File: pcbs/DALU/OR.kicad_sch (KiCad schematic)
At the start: 3 parts, among them U701 74HC32, U702 74HC32, U703 74HC245

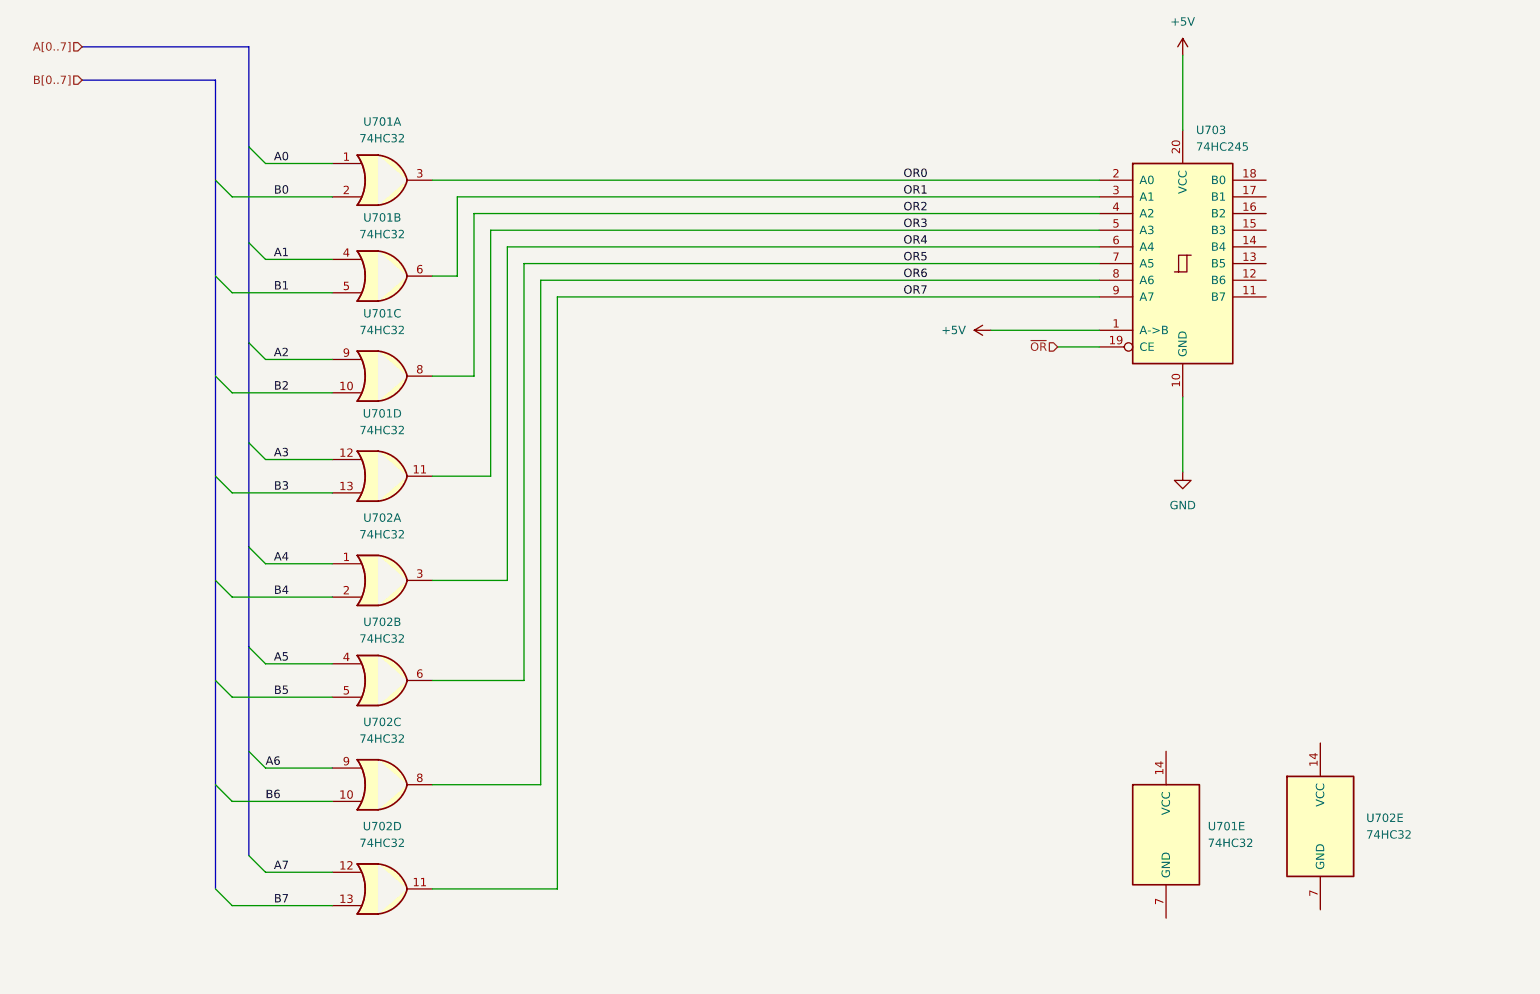
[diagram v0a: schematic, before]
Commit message: Routing.... have realised that I need to think more about vias
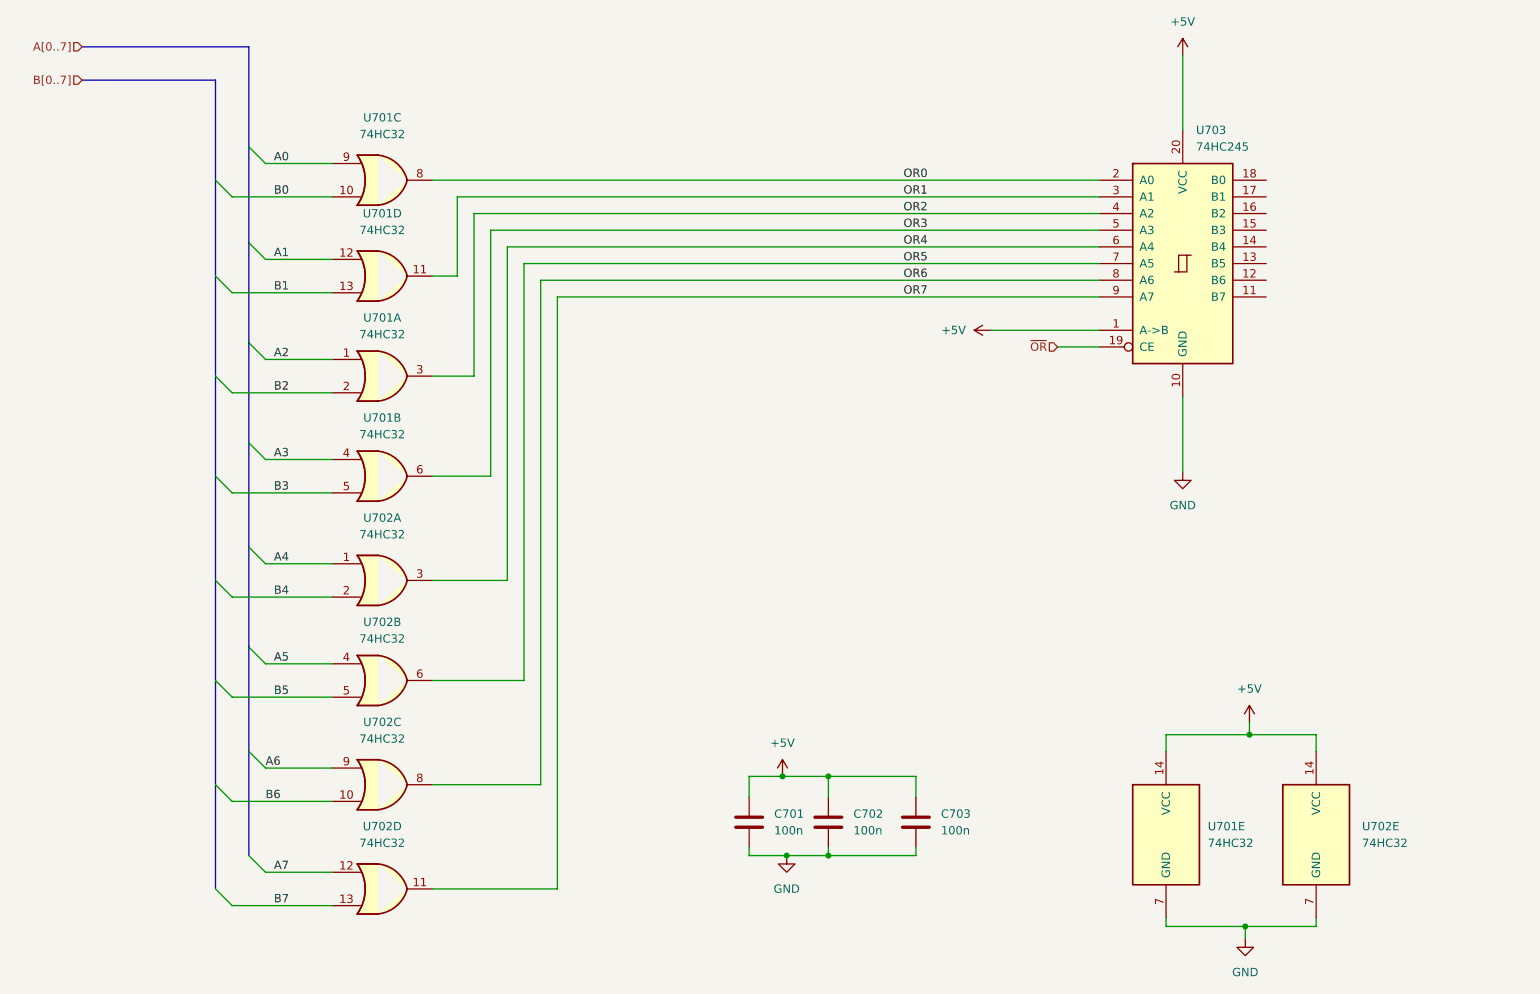
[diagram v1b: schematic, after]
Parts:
- added C701, C702, C703: 100n, Capacitor_SMD:C_0603_1608Metric, symbol Device:C
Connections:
- net +5V: now also U701.14 (VCC), U702.14 (VCC), C701.1, C702.1, C703.1
- net A0: now also U701.9; no longer U701.1
- net A1: now also U701.12; no longer U701.4
- net A2: now also U701.1; no longer U701.9
- net A3: now also U701.4; no longer U701.12
- net B0: now also U701.10; no longer U701.2
- net B1: now also U701.13; no longer U701.5
- net B2: now also U701.2; no longer U701.10
- net B3: now also U701.5; no longer U701.13
- net GND: now also U701.7 (GND), U702.7 (GND), C701.2, C702.2, C703.2
- net OR0: now also U701.8; no longer U701.3
- net OR1: now also U701.11; no longer U701.6
- net OR2: now also U701.3; no longer U701.8
- net OR3: now also U701.6; no longer U701.11
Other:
- moved on the sheet: U701A, U701B, U701C, U701D, U702E

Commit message: More rerouting
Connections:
- net RESULT7: now reaches U703.11 (B7)
- net RESULT6: now reaches U703.12 (B6)
- net RESULT5: now reaches U703.13 (B5)
- net RESULT4: now reaches U703.14 (B4)
- net RESULT3: now reaches U703.15 (B3)
- net RESULT2: now reaches U703.16 (B2)
- net RESULT1: now reaches U703.17 (B1)
- net RESULT0: now reaches U703.18 (B0)
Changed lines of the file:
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@@
   (junction (at 215.9 130.175) (diameter 0) (color 0 0 0 0)
   )
+  (bus_entry (at 234.315 60.96) (size -2.54 2.54)
+    (stroke (width 0) (type default) (color 0 0 0 0))
+  )
+  (bus_entry (at 234.315 53.34) (size -2.54 2.54)
+    (stroke (width 0) (type default) (color 0 0 0 0))
+  )
   (bus_entry (at 63.5 70.485) (size 2.54 2.54)
     (stroke (width 0) (type default) (color 0 0 0 0))
   )
+  (bus_entry (at 234.315 43.18) (size -2.54 2.54)
+    (stroke (width 0) (type default) (color 0 0 0 0))
+  )
   (bus_entry (at 58.42 106.68) (size 2.54 2.54)
     (stroke (width 0) (type default) (color 0 0 0 0))
   )
+  (bus_entry (at 234.315 58.42) (size -2.54 2.54)
+    (stroke (width 0) (type default) (color 0 0 0 0))
+  )
   (bus_entry (at 63.5 55.245) (size 2.54 2.54)
     (stroke (width 0) (type default) (color 0 0 0 0))
@@
     (stroke (width 0) (type default) (color 0 0 0 0))
   )
+  (bus_entry (at 234.315 45.72) (size -2.54 2.54)
+    (stroke (width 0) (type default) (color 0 0 0 0))
+  )
   (bus_entry (at 63.5 132.715) (size 2.54 2.54)
     (stroke (width 0) (type default) (color 0 0 0 0))
@@
     (stroke (width 0) (type default) (color 0 0 0 0))
   )
+  (bus_entry (at 234.315 48.26) (size -2.54 2.54)
+    (stroke (width 0) (type default) (color 0 0 0 0))
+  )
   (bus_entry (at 58.42 121.92) (size 2.54 2.54)
     (stroke (width 0) (type default) (color 0 0 0 0))
   )
+  (bus_entry (at 234.315 55.88) (size -2.54 2.54)
+    (stroke (width 0) (type default) (color 0 0 0 0))
+  )
   (bus_entry (at 58.42 45.72) (size 2.54 2.54)
     (stroke (width 0) (type default) (color 0 0 0 0))
@@
     (stroke (width 0) (type default) (color 0 0 0 0))
   )
+  (bus_entry (at 234.315 50.8) (size -2.54 2.54)
+    (stroke (width 0) (type default) (color 0 0 0 0))
+  )
   (wire (pts (xy 91.44 121.92) (xy 105.41 121.92))
     (stroke (width 0) (type default) (color 0 0 0 0))
   )
+  (bus (pts (xy 234.315 48.26) (xy 234.315 50.8))
+    (stroke (width 0) (type default) (color 0 0 0 0))
+  )
   (wire (pts (xy 91.44 60.325) (xy 95.25 60.325))
     (stroke (width 0) (type default) (color 0 0 0 0))
@@
     (stroke (width 0) (type default) (color 0 0 0 0))
   )
+  (wire (pts (xy 218.44 55.88) (xy 231.775 55.88))
+    (stroke (width 0) (type default) (color 0 0 0 0))
+  )
+  (wire (pts (xy 218.44 53.34) (xy 231.775 53.34))
+    (stroke (width 0) (type default) (color 0 0 0 0))
+  )
   (bus (pts (xy 58.42 137.795) (xy 58.42 153.67))
     (stroke (width 0) (type default) (color 0 0 0 0))
@@
     (stroke (width 0) (type default) (color 0 0 0 0))
   )
+  (wire (pts (xy 218.44 58.42) (xy 231.775 58.42))
+    (stroke (width 0) (type default) (color 0 0 0 0))
+  )
   (wire (pts (xy 165.1 136.525) (xy 165.1 139.7))
     (stroke (width 0) (type default) (color 0 0 0 0))
@@
     (stroke (width 0) (type default) (color 0 0 0 0))
   )
+  (bus (pts (xy 234.315 55.88) (xy 234.315 58.42))
+    (stroke (width 0) (type default) (color 0 0 0 0))
+  )
   (wire (pts (xy 107.95 137.795) (xy 91.44 137.795))
     (stroke (width 0) (type default) (color 0 0 0 0))
@@
     (stroke (width 0) (type default) (color 0 0 0 0))
   )
+  (bus (pts (xy 234.315 58.42) (xy 234.315 60.96))
+    (stroke (width 0) (type default) (color 0 0 0 0))
+  )
   (wire (pts (xy 60.96 140.335) (xy 76.2 140.335))
     (stroke (width 0) (type default) (color 0 0 0 0))
@@
     (stroke (width 0) (type default) (color 0 0 0 0))
   )
+  (wire (pts (xy 218.44 63.5) (xy 231.775 63.5))
+    (stroke (width 0) (type default) (color 0 0 0 0))
+  )
+  (bus (pts (xy 234.315 36.83) (xy 234.315 43.18))
+    (stroke (width 0) (type default) (color 0 0 0 0))
+  )
   (bus (pts (xy 63.5 101.6) (xy 63.5 116.84))
     (stroke (width 0) (type default) (color 0 0 0 0))
@@
     (stroke (width 0) (type default) (color 0 0 0 0))
   )
+  (bus (pts (xy 234.315 43.18) (xy 234.315 45.72))
+    (stroke (width 0) (type default) (color 0 0 0 0))
+  )
+  (wire (pts (xy 218.44 48.26) (xy 231.775 48.26))
+    (stroke (width 0) (type default) (color 0 0 0 0))
+  )
   (wire (pts (xy 145.415 148.59) (xy 151.765 148.59))
     (stroke (width 0) (type default) (color 0 0 0 0))
@@
     (stroke (width 0) (type default) (color 0 0 0 0))
   )
+  (bus (pts (xy 234.315 50.8) (xy 234.315 53.34))
+    (stroke (width 0) (type default) (color 0 0 0 0))
+  )
   (wire (pts (xy 100.33 53.34) (xy 100.33 90.805))
     (stroke (width 0) (type default) (color 0 0 0 0))
@@
     (stroke (width 0) (type default) (color 0 0 0 0))
   )
+  (bus (pts (xy 234.315 53.34) (xy 234.315 55.88))
+    (stroke (width 0) (type default) (color 0 0 0 0))
+  )
   (wire (pts (xy 60.96 124.46) (xy 76.2 124.46))
     (stroke (width 0) (type default) (color 0 0 0 0))
@@
     (stroke (width 0) (type default) (color 0 0 0 0))
   )
+  (bus (pts (xy 234.315 45.72) (xy 234.315 48.26))
+    (stroke (width 0) (type default) (color 0 0 0 0))
+  )
   (wire (pts (xy 97.79 50.8) (xy 97.79 75.565))
     (stroke (width 0) (type default) (color 0 0 0 0))
@@
     (stroke (width 0) (type default) (color 0 0 0 0))
   )
+  (wire (pts (xy 218.44 45.72) (xy 231.775 45.72))
+    (stroke (width 0) (type default) (color 0 0 0 0))
+  )
   (wire (pts (xy 102.87 55.88) (xy 102.87 106.68))
     (stroke (width 0) (type default) (color 0 0 0 0))
   )
+  (wire (pts (xy 218.44 50.8) (xy 231.775 50.8))
+    (stroke (width 0) (type default) (color 0 0 0 0))
+  )
   (bus (pts (xy 38.1 30.48) (xy 58.42 30.48))
     (stroke (width 0) (type default) (color 0 0 0 0))
@@
     (stroke (width 0) (type default) (color 0 0 0 0))
   )
+  (wire (pts (xy 218.44 60.96) (xy 231.775 60.96))
+    (stroke (width 0) (type default) (color 0 0 0 0))
+  )
   (wire (pts (xy 144.78 136.525) (xy 151.765 136.525))
     (stroke (width 0) (type default) (color 0 0 0 0))
@@
     (stroke (width 0) (type default) (color 0 0 0 0))
   )
+  (bus (pts (xy 241.3 36.83) (xy 234.315 36.83))
+    (stroke (width 0) (type default) (color 0 0 0 0))
+  )
   (label "B3" (at 67.31 93.345 0)
     (effects (font (size 1.27 1.27)) (justify left bottom))
@@
     (effects (font (size 1.27 1.27)) (justify left bottom))
   )
+  (label "RESULT4" (at 218.44 55.88 0)
+    (effects (font (size 1.27 1.27)) (justify left bottom))
+  )
+  (label "RESULT6" (at 218.44 60.96 0)
+    (effects (font (size 1.27 1.27)) (justify left bottom))
+  )
   (label "A2" (at 67.31 73.025 0)
     (effects (font (size 1.27 1.27)) (justify left bottom))
   )
+  (label "RESULT7" (at 218.44 63.5 0)
+    (effects (font (size 1.27 1.27)) (justify left bottom))
+  )
   (label "OR0" (at 163.195 45.72 0)
     (effects (font (size 1.27 1.27)) (justify left bottom))
@@
     (effects (font (size 1.27 1.27)) (justify left bottom))
   )
+  (label "RESULT1" (at 218.44 48.26 0)
+    (effects (font (size 1.27 1.27)) (justify left bottom))
+  )
+  (label "RESULT2" (at 218.44 50.8 0)
+    (effects (font (size 1.27 1.27)) (justify left bottom))
+  )
   (label "B6" (at 66.04 140.335 0)
     (effects (font (size 1.27 1.27)) (justify left bottom))
@@
     (effects (font (size 1.27 1.27)) (justify left bottom))
   )
+  (label "RESULT5" (at 218.44 58.42 0)
+    (effects (font (size 1.27 1.27)) (justify left bottom))
+  )
   (label "B4" (at 67.31 109.22 0)
     (effects (font (size 1.27 1.27)) (justify left bottom))
@@
   )
   (label "OR4" (at 163.195 55.88 0)
+    (effects (font (size 1.27 1.27)) (justify left bottom))
+  )
+  (label "RESULT3" (at 218.44 53.34 0)
+    (effects (font (size 1.27 1.27)) (justify left bottom))
+  )
+  (label "RESULT0" (at 218.44 45.72 0)
     (effects (font (size 1.27 1.27)) (justify left bottom))
   )
@@
     (effects (font (size 1.27 1.27)) (justify right))
   )
+  (hierarchical_label "RESULT[0..7]" (shape tri_state) (at 241.3 36.83 0)
+    (effects (font (size 1.27 1.27)) (justify left))
+  )
   (hierarchical_label "~{OR}" (shape input) (at 186.69 71.12 180)

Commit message: Sending for production
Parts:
- U701, U702: now left out of the parts list
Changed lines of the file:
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@@
   )
   (symbol (lib_id "74xx:74LS32") (at 83.82 90.805 0) (unit 2)
-    (in_bom yes) (on_board yes) (fields_autoplaced)
+    (in_bom no) (on_board yes) (fields_autoplaced)
     (property "Reference" "U701" (id 0) (at 83.82 81.915 0))
     (property "Value" "74HC32" (id 1) (at 83.82 84.455 0))
@@
   )
   (symbol (lib_id "74xx:74LS32") (at 83.82 45.72 0) (unit 3)
-    (in_bom yes) (on_board yes) (fields_autoplaced)
+    (in_bom no) (on_board yes) (fields_autoplaced)
     (property "Reference" "U701" (id 0) (at 83.82 36.195 0))
     (property "Value" "74HC32" (id 1) (at 83.82 38.735 0))
@@
   )
   (symbol (lib_id "74xx:74LS32") (at 203.2 145.415 0) (unit 5)
-    (in_bom yes) (on_board yes) (fields_autoplaced)
+    (in_bom no) (on_board yes) (fields_autoplaced)
     (property "Reference" "U701" (id 0) (at 209.55 144.1449 0)
       (effects (font (size 1.27 1.27)) (justify left))
@@
   )
   (symbol (lib_id "74xx:74LS32") (at 83.82 106.68 0) (unit 1)
-    (in_bom yes) (on_board yes) (fields_autoplaced)
+    (in_bom no) (on_board yes) (fields_autoplaced)
     (property "Reference" "U702" (id 0) (at 83.82 97.155 0))
     (property "Value" "74HC32" (id 1) (at 83.82 99.695 0))
@@
   )
   (symbol (lib_id "74xx:74LS32") (at 83.82 121.92 0) (unit 2)
-    (in_bom yes) (on_board yes) (fields_autoplaced)
+    (in_bom no) (on_board yes) (fields_autoplaced)
     (property "Reference" "U702" (id 0) (at 83.82 113.03 0))
     (property "Value" "74HC32" (id 1) (at 83.82 115.57 0))
@@
   )
   (symbol (lib_id "74xx:74LS32") (at 83.82 75.565 0) (unit 1)
-    (in_bom yes) (on_board yes) (fields_autoplaced)
+    (in_bom no) (on_board yes) (fields_autoplaced)
     (property "Reference" "U701" (id 0) (at 83.82 66.675 0))
     (property "Value" "74HC32" (id 1) (at 83.82 69.215 0))
@@
   )
   (symbol (lib_id "74xx:74LS32") (at 83.82 153.67 0) (unit 4)
-    (in_bom yes) (on_board yes) (fields_autoplaced)
+    (in_bom no) (on_board yes) (fields_autoplaced)
     (property "Reference" "U702" (id 0) (at 83.82 144.145 0))
     (property "Value" "74HC32" (id 1) (at 83.82 146.685 0))
@@
   )
   (symbol (lib_id "74xx:74LS32") (at 226.06 145.415 0) (unit 5)
-    (in_bom yes) (on_board yes) (fields_autoplaced)
+    (in_bom no) (on_board yes) (fields_autoplaced)
     (property "Reference" "U702" (id 0) (at 233.045 144.1449 0)
       (effects (font (size 1.27 1.27)) (justify left))
@@
   )
   (symbol (lib_id "74xx:74LS32") (at 83.82 60.325 0) (unit 4)
-    (in_bom yes) (on_board yes) (fields_autoplaced)
+    (in_bom no) (on_board yes) (fields_autoplaced)
     (property "Reference" "U701" (id 0) (at 83.82 50.8 0))
     (property "Value" "74HC32" (id 1) (at 83.82 53.34 0))
@@
   )
   (symbol (lib_id "74xx:74LS32") (at 83.82 137.795 0) (unit 3)
-    (in_bom yes) (on_board yes) (fields_autoplaced)
+    (in_bom no) (on_board yes) (fields_autoplaced)
     (property "Reference" "U702" (id 0) (at 83.82 128.27 0))
     (property "Value" "74HC32" (id 1) (at 83.82 130.81 0))
